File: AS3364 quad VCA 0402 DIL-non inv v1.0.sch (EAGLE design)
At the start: 44 parts, among them IC1 TL072JD, IC2 TL072JD

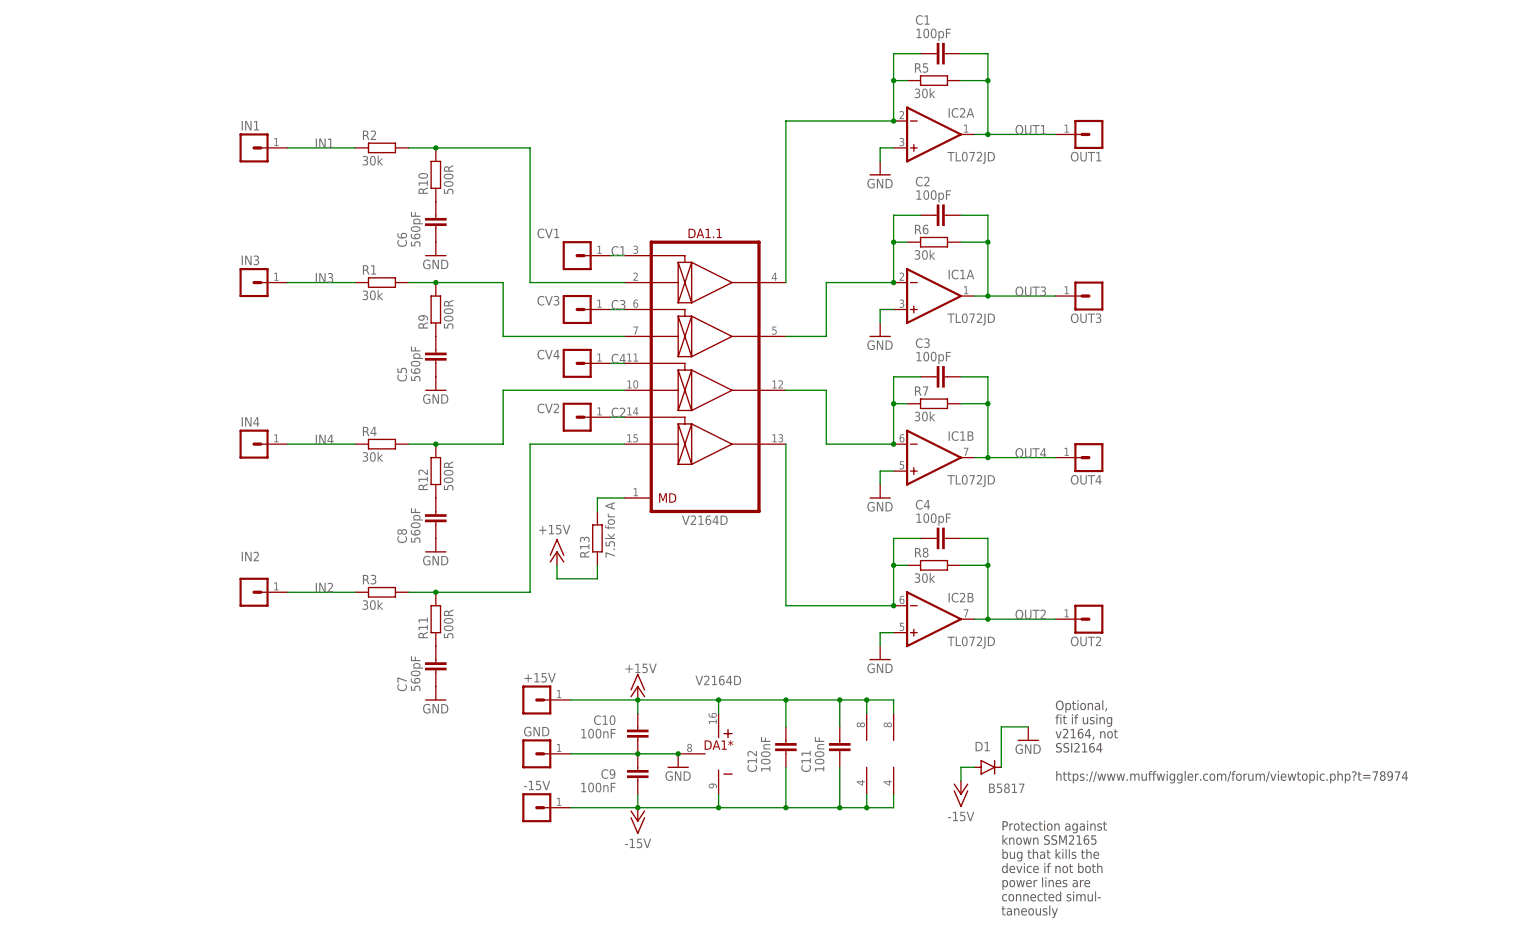
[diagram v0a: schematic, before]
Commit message: Added AS3364 versions of quad VCA
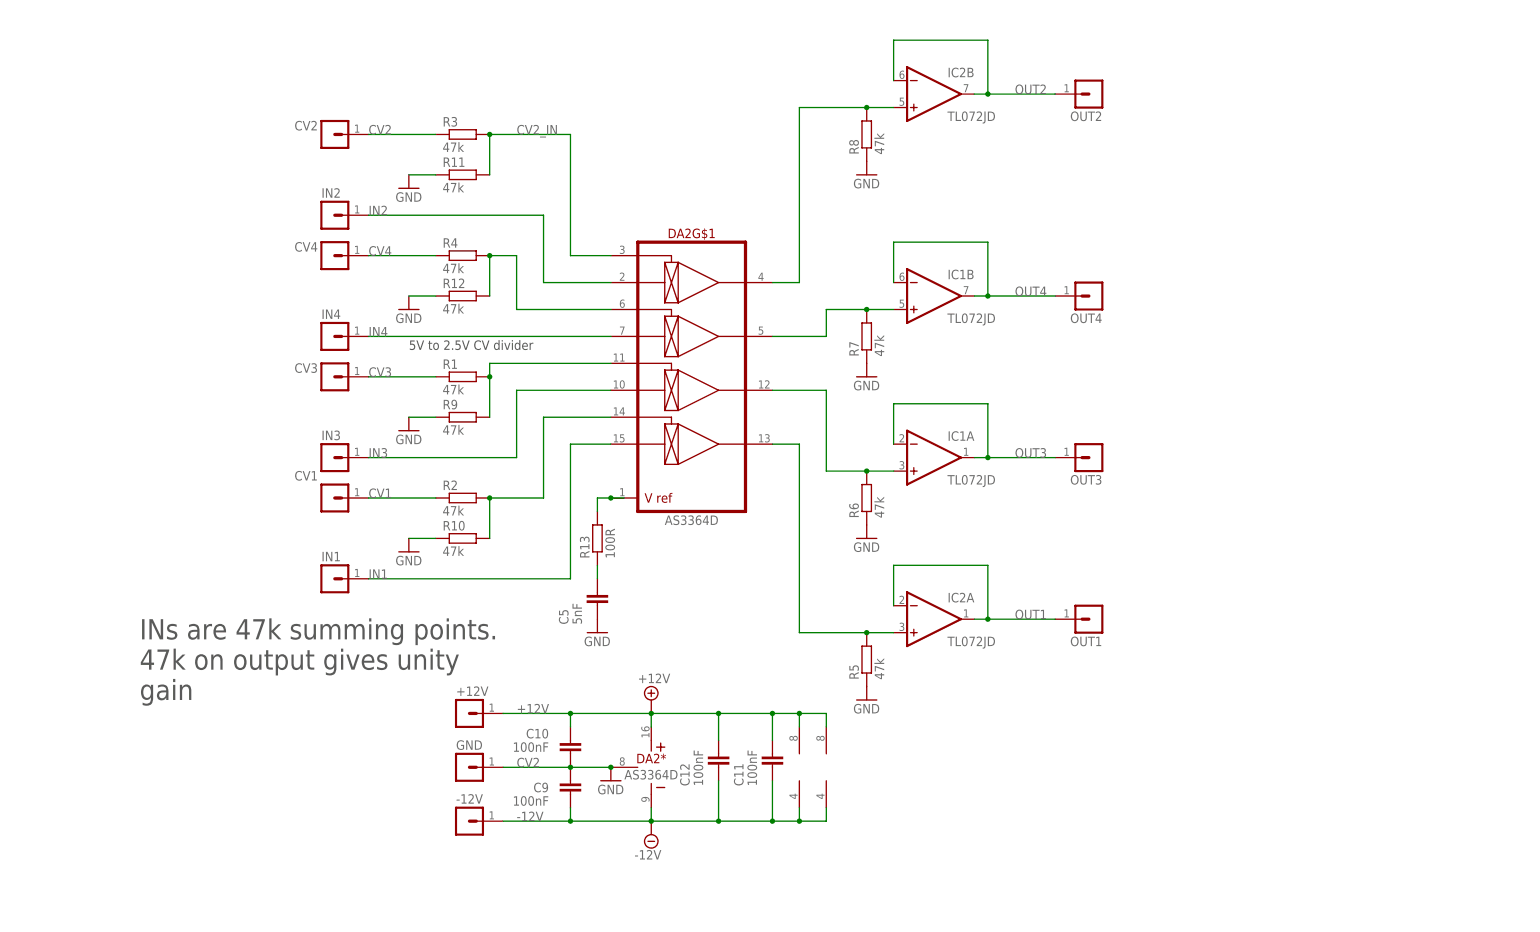
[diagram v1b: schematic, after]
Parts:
- removed +15V, -15V: (no value), joakim:MA01-1JP
- removed C1, C2, C3, C4: 100pF, rcl:C-EUC0402
- removed C6, C7, C8: 560pF, rcl:C-EUC0603
- removed D1: B5817, diode:DIODE-SOD323-R
- removed DA1: V2164D, ic-coolaudio:V2164D
- added +12V, -12V: (no value), joakim:MA01-1JP
- added DA2: AS3364D, joakim:AS3364D
- C5: value 560pF -> 5nF; device rcl:C-EUC0603 -> rcl:C-EUC0402
- R1, R2, R3, R4, R5, R6, R7, R8: value 30k -> 47k
- R10, R11, R12, R9: value 500R -> 47k
- R13: value 7.5k for A -> 100R
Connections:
- removed net +15V: +15V.1, C10.2, C11.2, C12.2, DA1*.V+, IC1P.V+, IC2P.V+, R13.1
- removed net -15V: -15V.1, C11.1, C12.1, C9.1, D1.A, DA1*.V-, IC1P.V-, IC2P.V-
- removed net C1: CV1.1, DA1.1.CV1
- removed net C2: CV2.1, DA1.1.CV4
- removed net C3: CV3.1, DA1.1.CV2
- removed net C4: CV4.1, DA1.1.CV3
- removed net N$1: C4.1, DA1.1.OUT4, IC2B.-IN, R8.1
- removed net N$17: DA1.1.IN2, R1.2, R9.2
- removed net N$18: DA1.1.IN1, R10.2, R2.2
- removed net N$19: DA1.1.IN4, R11.2, R3.2
- removed net N$20: DA1.1.IN3, R12.2, R4.2
- removed net N$3: C3.1, DA1.1.OUT3, IC1B.-IN, R7.1
- removed net N$5: C2.1, DA1.1.OUT2, IC1A.-IN, R6.1
- removed net N$7: C1.1, DA1.1.OUT1, IC2A.-IN, R5.1
- removed net N$9: C5.2, R9.1
- new net +12V: +12V.1, C10.2, C11.2, C12.2, DA2*.V+, IC1P.V+, IC2P.V+
- new net -12V: -12V.1, C11.1, C12.1, C9.1, DA2*.V-, IC1P.V-, IC2P.V-
- new net CV1: CV1.1, R2.1
- new net CV2: CV2.1, R3.1
- new net CV2_IN: DA2G$1.CV1, R11.2, R3.2
- new net CV3: CV3.1, R1.1
- new net CV4: CV4.1, R4.1
- new net N$13: DA2G$1.OUT4, IC2A.+IN, R5.2
- new net N$14: C5.2, R13.1
- new net N$21: DA2G$1.CV4, R10.2, R2.2
- new net N$4: DA2G$1.OUT1, IC2B.+IN, R8.2
- new net N$6: DA2G$1.OUT2, IC1B.+IN, R7.2
- net GND: now also DA2*.GND, R10.1, R11.1, R12.1, R5.1, R6.1, R7.1, R8.1, R9.1; no longer C6.1, C7.1, C8.1, D1.C, DA1*.GND, IC1A.+IN, IC1B.+IN, IC2A.+IN, IC2B.+IN
- net IN1: now also DA2G$1.IN4; no longer R2.1
- net IN2: now also DA2G$1.IN1; no longer R3.1
- net IN3: now also DA2G$1.IN3; no longer R1.1
- net IN4: now also DA2G$1.IN2; no longer R4.1
- net N$10: now also DA2G$1.CV2, R12.2, R4.2; no longer C6.2, R10.1
- net N$11: now also DA2G$1.OUT3, IC1A.+IN, R6.2; no longer C7.2, R11.1
- net N$12: now also DA2G$1.CV3, R1.2, R9.2; no longer C8.2, R12.1
- net N$2: now also DA2G$1.VREF; no longer DA1.1.MD
- net OUT1: now also IC2A.-IN; no longer C1.2, R5.2
- net OUT2: now also IC2B.-IN; no longer C4.2, R8.2
- net OUT3: now also IC1A.-IN; no longer C2.2, R6.2
- net OUT4: now also IC1B.-IN; no longer C3.2, R7.2
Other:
- note added: "5V to 2.5V CV divider"
- note added: "INs are 47k summing points. 47k on output gives unity gain"
- note removed: "Optional, fit if using v2164, not SSI2164 https://www.muffwiggler.com/forum/viewtopic.php?t=78974"
- note removed: "Protection against known SSM2165 bug that kills the device if not both power lines are connected simul- taneously"
- moved on the sheet: C10, C11, C12, C5, C9, CV1, CV2, CV3, CV4, GND, IC1A, IC1B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

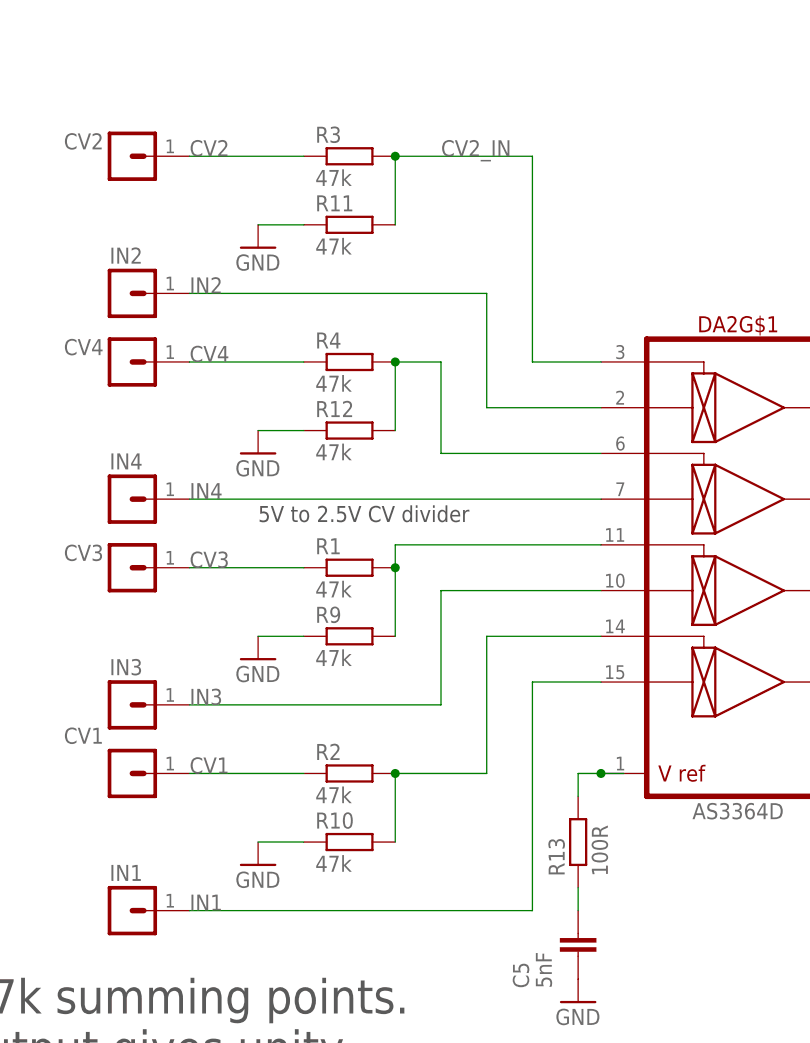
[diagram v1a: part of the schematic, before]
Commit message: Checked most things, changed CV input resistors, added cap to mixer output
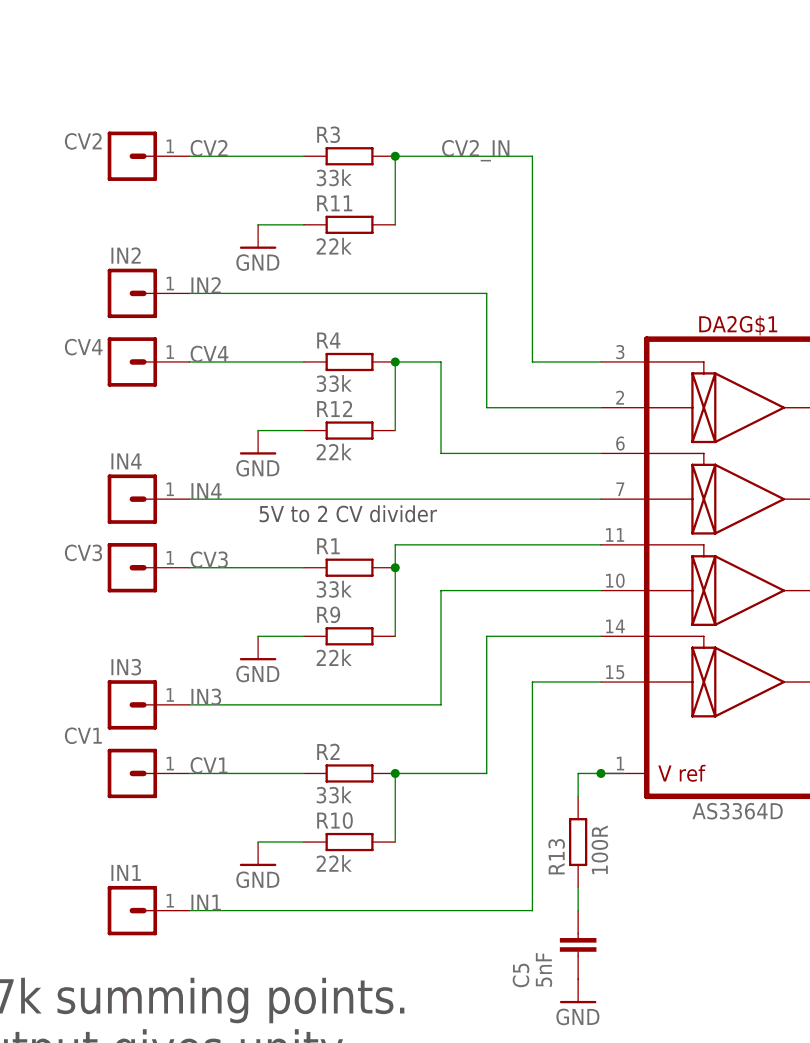
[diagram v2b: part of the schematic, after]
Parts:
- R1, R2, R3, R4: value 47k -> 33k
- R10, R11, R12, R9: value 47k -> 22k
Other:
- note added: "5V to 2 CV divider"
- note removed: "5V to 2.5V CV divider"
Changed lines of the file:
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@@
 </classes>
 <parts>
-<part name="R1" library="rcl" library_urn="urn:adsk.eagle:library:334" deviceset="R-EU_" device="R0402" package3d_urn="urn:adsk.eagle:package:23547/3" value="47k"/>
-<part name="R2" library="rcl" library_urn="urn:adsk.eagle:library:334" deviceset="R-EU_" device="R0402" package3d_urn="urn:adsk.eagle:package:23547/3" value="47k"/>
-<part name="R3" library="rcl" library_urn="urn:adsk.eagle:library:334" deviceset="R-EU_" device="R0402" package3d_urn="urn:adsk.eagle:package:23547/3" value="47k"/>
-<part name="R4" library="rcl" library_urn="urn:adsk.eagle:library:334" deviceset="R-EU_" device="R0402" package3d_urn="urn:adsk.eagle:package:23547/3" value="47k"/>
+<part name="R1" library="rcl" library_urn="urn:adsk.eagle:library:334" deviceset="R-EU_" device="R0402" package3d_urn="urn:adsk.eagle:package:23547/3" value="33k"/>
+<part name="R2" library="rcl" library_urn="urn:adsk.eagle:library:334" deviceset="R-EU_" device="R0402" package3d_urn="urn:adsk.eagle:package:23547/3" value="33k"/>
+<part name="R3" library="rcl" library_urn="urn:adsk.eagle:library:334" deviceset="R-EU_" device="R0402" package3d_urn="urn:adsk.eagle:package:23547/3" value="33k"/>
+<part name="R4" library="rcl" library_urn="urn:adsk.eagle:library:334" deviceset="R-EU_" device="R0402" package3d_urn="urn:adsk.eagle:package:23547/3" value="33k"/>
 <part name="R5" library="rcl" library_urn="urn:adsk.eagle:library:334" deviceset="R-EU_" device="R0402" package3d_urn="urn:adsk.eagle:package:23547/3" value="47k"/>
 <part name="R6" library="rcl" library_urn="urn:adsk.eagle:library:334" deviceset="R-EU_" device="R0402" package3d_urn="urn:adsk.eagle:package:23547/3" value="47k"/>
 <part name="R7" library="rcl" library_urn="urn:adsk.eagle:library:334" deviceset="R-EU_" device="R0402" package3d_urn="urn:adsk.eagle:package:23547/3" value="47k"/>
 <part name="R8" library="rcl" library_urn="urn:adsk.eagle:library:334" deviceset="R-EU_" device="R0402" package3d_urn="urn:adsk.eagle:package:23547/3" value="47k"/>
-<part name="R9" library="rcl" library_urn="urn:adsk.eagle:library:334" deviceset="R-EU_" device="R0402" package3d_urn="urn:adsk.eagle:package:23547/3" value="47k"/>
-<part name="R10" library="rcl" library_urn="urn:adsk.eagle:library:334" deviceset="R-EU_" device="R0402" package3d_urn="urn:adsk.eagle:package:23547/3" value="47k"/>
-<part name="R11" library="rcl" library_urn="urn:adsk.eagle:library:334" deviceset="R-EU_" device="R0402" package3d_urn="urn:adsk.eagle:package:23547/3" value="47k"/>
-<part name="R12" library="rcl" library_urn="urn:adsk.eagle:library:334" deviceset="R-EU_" device="R0402" package3d_urn="urn:adsk.eagle:package:23547/3" value="47k"/>
+<part name="R9" library="rcl" library_urn="urn:adsk.eagle:library:334" deviceset="R-EU_" device="R0402" package3d_urn="urn:adsk.eagle:package:23547/3" value="22k"/>
+<part name="R10" library="rcl" library_urn="urn:adsk.eagle:library:334" deviceset="R-EU_" device="R0402" package3d_urn="urn:adsk.eagle:package:23547/3" value="22k"/>
+<part name="R11" library="rcl" library_urn="urn:adsk.eagle:library:334" deviceset="R-EU_" device="R0402" package3d_urn="urn:adsk.eagle:package:23547/3" value="22k"/>
+<part name="R12" library="rcl" library_urn="urn:adsk.eagle:library:334" deviceset="R-EU_" device="R0402" package3d_urn="urn:adsk.eagle:package:23547/3" value="22k"/>
 <part name="C9" library="rcl" library_urn="urn:adsk.eagle:library:334" deviceset="C-EU" device="C0402" package3d_urn="urn:adsk.eagle:package:23626/2" value="100nF"/>
 <part name="C10" library="rcl" library_urn="urn:adsk.eagle:library:334" deviceset="C-EU" device="C0402" package3d_urn="urn:adsk.eagle:package:23626/2" value="100nF"/>
@@
 47k on output gives unity
 gain</text>
-<text x="5.08" y="58.42" size="1.778" layer="97">5V to 2.5V CV divider</text>
+<text x="5.08" y="58.42" size="1.778" layer="97">5V to 2 CV divider</text>
 </plain>
 <instances>
